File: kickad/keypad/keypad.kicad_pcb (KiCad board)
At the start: 2 copper layers, 124 x 130 mm, 23 parts

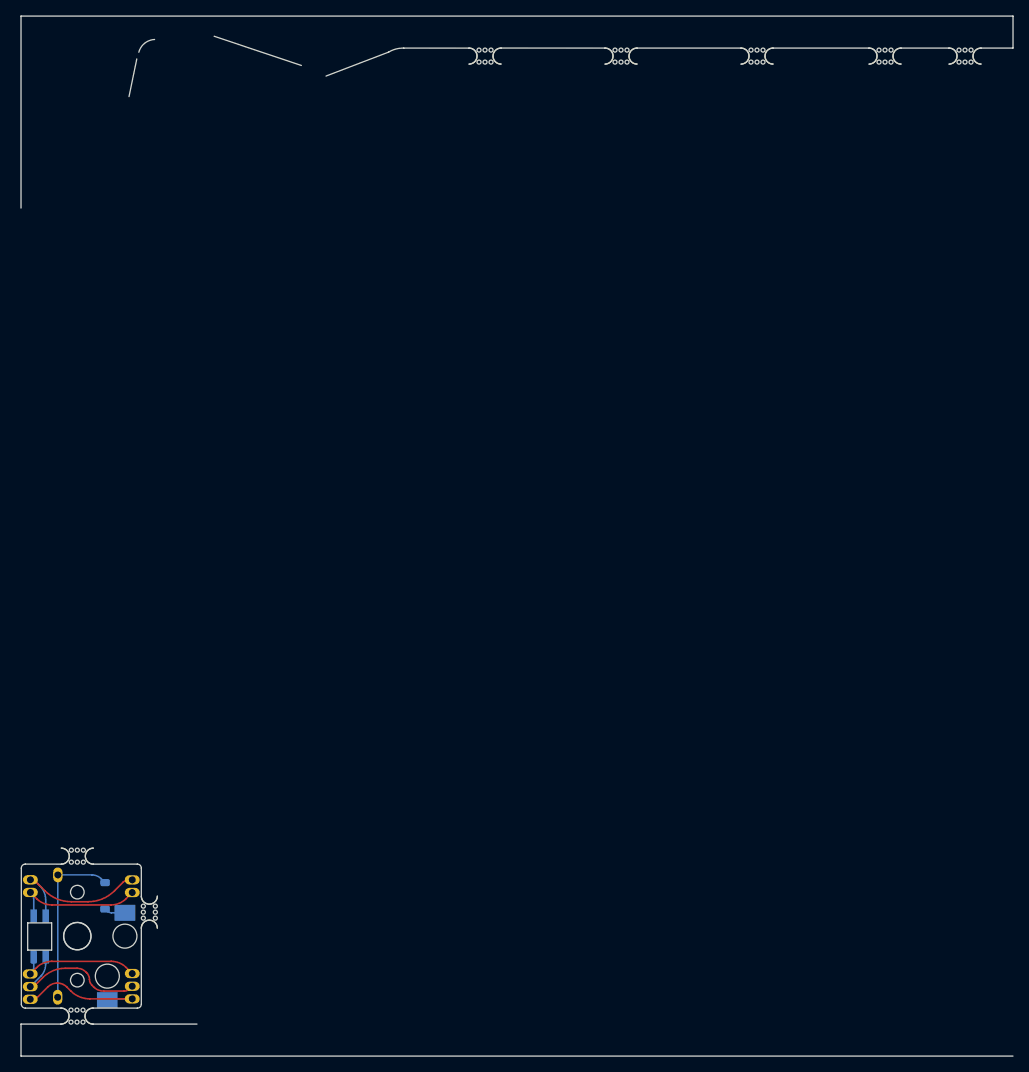
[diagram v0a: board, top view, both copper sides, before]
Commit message: Reworking the keypad PCB
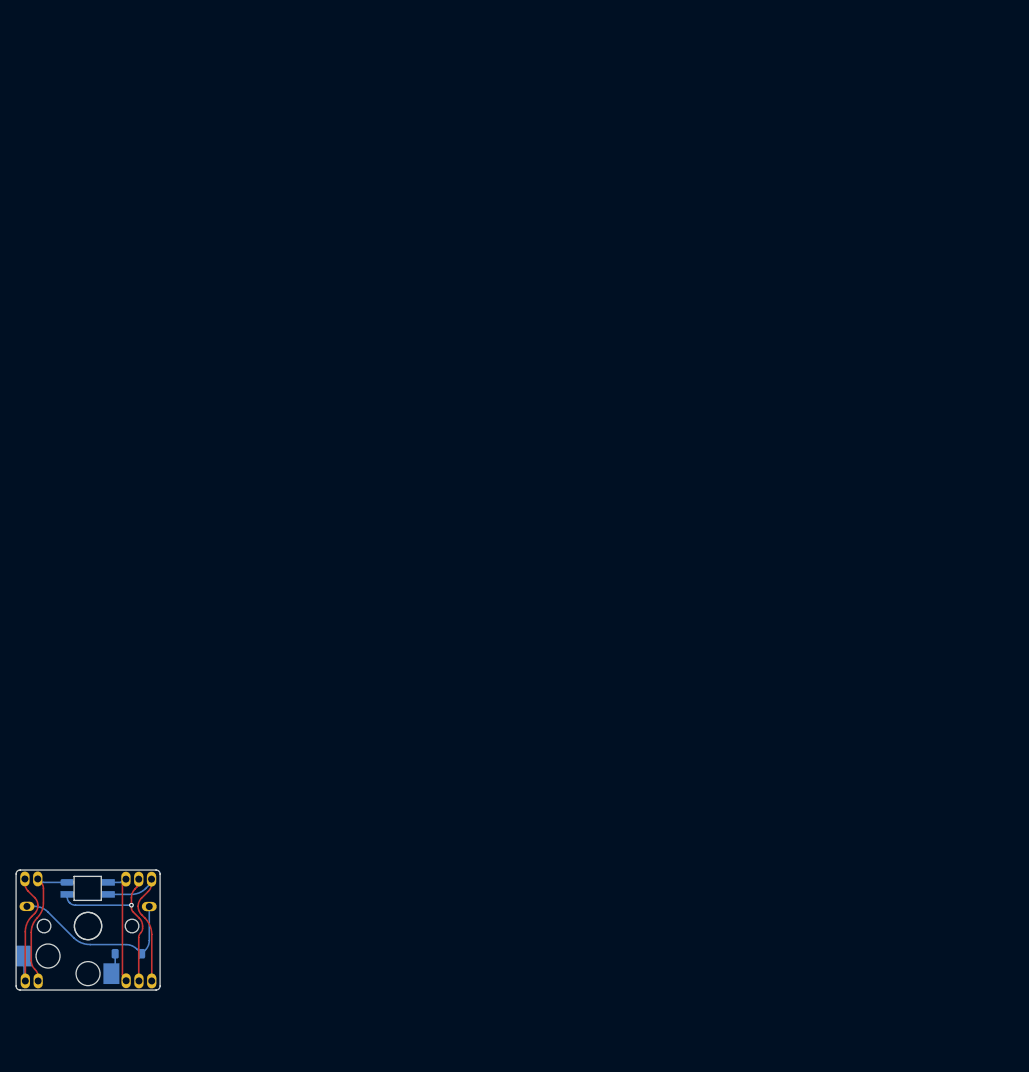
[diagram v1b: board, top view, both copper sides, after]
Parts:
- removed mouse-bite-2mm-slot (x8): VAL**, Panelization:mouse-bite-2mm-slot
- moved ? 19.1 mm to (94.7, 133.9), turned to 0 degrees
- moved ? 15.1 mm to (96.3, 133.9), turned to 0 degrees
- moved ? 15.1 mm to (80.5, 133.9), turned to 0 degrees
- moved ? 13.6 mm to (80.5, 146.6), turned to 0 degrees
- moved ? 12.9 mm to (96.3, 146.6), turned to 0 degrees
- moved ? 12.1 mm to (96.0, 137.3), turned to 180 degrees
- moved ? 12.1 mm to (93.1, 133.9), turned to 0 degrees
- moved ? 12.0 mm to (80.7, 137.3), turned to 180 degrees
- moved ? 11.9 mm to (82.1, 133.9), turned to 90 degrees
- moved ? 11.8 mm to (82.1, 146.6), turned to 90 degrees
- moved ? 11.1 mm to (93.1, 146.6), turned to 0 degrees
- moved D2 8.50 mm to (88.3, 135.0), turned to 0 degrees
- moved D1 7.81 mm to (93.4, 143.2), turned to 180 degrees
- moved S1 1.84 mm to (88.4, 139.7), turned to 0 degrees
- moved ? 1.07 mm to (94.7, 146.6), turned to 0 degrees
- renumbered D16 to D1, D18 to D2, S16 to S1
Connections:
- ? pad : VCC -> VSS (x2)
- ? pad : Row -> ROW (x2)
- ? pad : Col -> COL (x2)
- D1 pad 1: Row 1 L -> ROW
- D2 pad 1: VCC L -> VSS
- D2 pad 2: unconnected-(D18-DOUT-Pad2) -> OUT
- D2 pad 3: GND L -> GND
- D2 pad 4: Net-(D18-DIN) -> IN
- S1 pad 1: Col 0 L -> COL
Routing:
- net ROW: track 0.00 -> 22.7 mm
- net Row: track 21.3 -> 0.00 mm
- net VSS: track 0.00 -> 20.1 mm
- net VCC: track 19.9 -> 0.00 mm
- net Col: track 17.2 -> 0.00 mm
- net COL: track 0.00 -> 16.9 mm
- net IN: track 19.5 -> 23.0 mm, vias 0 -> 1
- net OUT: track 16.9 -> 15.4 mm
- net GND: track 16.0 -> 17.4 mm
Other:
- board size 124 x 130 mm -> 18 x 15 mm
